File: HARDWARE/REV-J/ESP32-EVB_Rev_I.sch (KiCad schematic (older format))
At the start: 151 parts, among them CON1 TB3 DG306-5.0-3P, CON2 TB3 DG306-5.0-3P, Q1 BC817-40(SOT23), Q2 BC817-40(SOT23), Q3 Q12MHz/20pF/30ppm/2P/HC-49SM(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, Q4 BC817-40(SOT23), Q5 BC817-40(SOT23), Q7 BC817-40(SOT23), U1 BL4054B-42TPRN(SOT23-5), U10 BAT54C(SOT23-3), U2 SY8089AAAC(SOT23-5), U3 ESP-WROOM-32, U4 LAN8710A-EZC(QFN32), U5 CH340T(SSOP20W), U6 MCP2562-E/SN(SOIC-8_150mil), U7 RPM7236-H8, U8 NCP303LSN27T1G(SOT-23-5), U9 BAT54C(SOT23-3)

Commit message: Update 434121043836 (rev1).stp, 5040771891.stp, and 173 more files...
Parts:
- removed 5.0V/3.3V2: Closed(1-2)/Opened(2-3), OLIMEX_Jumpers-FP:SJ_2_SMALL_12_TIED, symbol ESP32-EVB_Rev_I:SJ2W_Closed(1-2)
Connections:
- net labels removed: vm
- wire segments 689 -> 690
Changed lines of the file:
@@
 	13900 13400 13900 13900
 Connection ~ 13900 13900
-Connection ~ 13700 13900
-Wire Wire Line
-	13000 13900 13700 13900
 Wire Wire Line
 	15600 13700 13000 13700
@@
 	13000 14000 15600 14000
 Wire Wire Line
-	13000 13800 13500 13800
-Wire Wire Line
-	13500 13800 13500 14900
+	13000 13800 13150 13800
 Wire Wire Line
 	19900 7800 18800 7800
@@
 	12400 14000 11600 14000
 Wire Wire Line
+	11600 14000 11600 14400
+Wire Wire Line
+	11600 14400 12600 14400
+Wire Wire Line
 	2900 1800 2900 2100
 Wire Wire Line
@@
 Wire Wire Line
 	13700 13900 13700 14500
+$Comp
+L ESP32-EVB_Rev_I:+3.3V #PWR0101
+U 1 1 5B27C8D3
+P 12600 14400
+F 0 "#PWR0101" H 12600 14250 50  0001 C CNN
+F 1 "+3.3V" V 12600 14525 50  0000 L CNN
+F 2 "" H 12600 14400 60  0000 C CNN
+F 3 "" H 12600 14400 60  0000 C CNN
+	1    12600 14400
+	0    1    1    0
+$EndComp
 $Comp
 L ESP32-EVB_Rev_I:MCP2562-E_SN(SOIC-8_150mil) U6
@@
 	-1   0    0    1
 $EndComp
-$Comp
-L ESP32-EVB_Rev_I:SJ2W_Closed(1-2) 5.0V/3.3V2
-U 1 1 6188D1A4
-P 12350 14650
-F 0 "5.0V/3.3V2" V 12650 14400 50  0000 L BNN
-F 1 "Closed(1-2)/Opened(2-3)" V 12550 14100 50  0000 L BNN
-F 2 "OLIMEX_Jumpers-FP:SJ_2_SMALL_12_TIED" H 12380 14800 20  0001 C CNN
-F 3 "" H 12350 14650 60  0000 C CNN
-	1    12350 14650
-	1    0    0    1
-$EndComp
-$Comp
-L ESP32-EVB_Rev_I:+3.3V #PWR0101
-U 1 1 5B27C8D3
-P 12350 14450
-F 0 "#PWR0101" H 12350 14300 50  0001 C CNN
-F 1 "+3.3V" H 12050 14500 50  0000 L CNN
-F 2 "" H 12350 14450 60  0000 C CNN
-F 3 "" H 12350 14450 60  0000 C CNN
-	1    12350 14450
-	1    0    0    -1
-$EndComp
-Wire Wire Line
-	12150 14650 11600 14650
-Wire Wire Line
-	11600 14000 11600 14650
-$Comp
-L ESP32-EVB_Rev_I:GND #PWR0114
-U 1 1 61ADEB7D
-P 12350 14850
-F 0 "#PWR0114" H 12350 14600 50  0001 C CNN
-F 1 "GND" H 12350 14700 50  0000 C CNN
-F 2 "" H 12350 14850 60  0000 C CNN
-F 3 "" H 12350 14850 60  0000 C CNN
-	1    12350 14850
-	1    0    0    -1
-$EndComp
-Connection ~ 11000 13800
+Wire Wire Line
+	13000 13900 13150 13900
+Wire Wire Line
+	13150 13800 13150 13900
+Wire Wire Line
+	11500 13600 11800 13600
+Connection ~ 11500 13600
+Connection ~ 11800 13600
 $Comp
 L ESP32-EVB_Rev_I:R R12
-U 1 1 61AF20A4
+U 1 1 61A8BD6D
 P 10850 13800
-F 0 "R12" H 10850 13800 50  0000 C CNN
-F 1 "10k/R0603" H 10750 13900 50  0000 C CNN
+F 0 "R12" H 11025 13850 50  0000 C CNN
+F 1 "10k/R0603" H 10525 13850 50  0000 C CNN
 F 2 "OLIMEX_RLC-FP:R_0603_5MIL_DWS" V 10780 13800 30  0001 C CNN
 F 3 "" H 10850 13800 30  0000 C CNN
 	1    10850 13800
-	1    0    0    1
-$EndComp
+	-1   0    0    -1
+$EndComp
+Connection ~ 11000 13800
 $Comp
 L ESP32-EVB_Rev_I:R R13
-U 1 1 61B8557C
-P 11000 14950
-F 0 "R13" H 11000 14950 50  0000 C CNN
-F 1 "10k/R0603" H 11100 14850 50  0000 C CNN
-F 2 "OLIMEX_RLC-FP:R_0603_5MIL_DWS" V 10930 14950 30  0001 C CNN
-F 3 "" H 11000 14950 30  0000 C CNN
-	1    11000 14950
-	0    -1   1    0
-$EndComp
-Connection ~ 11000 14800
-$Comp
-L ESP32-EVB_Rev_I:GND #PWR0115
-U 1 1 61B984EC
+U 1 1 61A8C506
+P 11650 14800
+F 0 "R13" H 11825 14850 50  0000 C CNN
+F 1 "10k/R0603" H 11325 14850 50  0000 C CNN
+F 2 "OLIMEX_RLC-FP:R_0603_5MIL_DWS" V 11580 14800 30  0001 C CNN
+F 3 "" H 11650 14800 30  0000 C CNN
+	1    11650 14800
+	-1   0    0    -1
+$EndComp
+Connection ~ 11500 14800
+$Comp
+L ESP32-EVB_Rev_I:GND #PWR0114
+U 1 1 61A8D549
 P 10700 13800
-F 0 "#PWR0115" H 10700 13550 50  0001 C CNN
-F 1 "GND" V 10700 13625 50  0000 C CNN
+F 0 "#PWR0114" H 10700 13550 50  0001 C CNN
+F 1 "GND" H 10700 13650 50  0000 C CNN
 F 2 "" H 10700 13800 60  0000 C CNN
 F 3 "" H 10700 13800 60  0000 C CNN
 	1    10700 13800
-	0    1    -1   0
-$EndComp
-Text GLabel 11000 15100 3    50   Input ~ 0
-vm
-Text Label 12300 13700 0    50   ~ 0
-vm
+	1    0    0    -1
+$EndComp
 $EndSCHEMATC

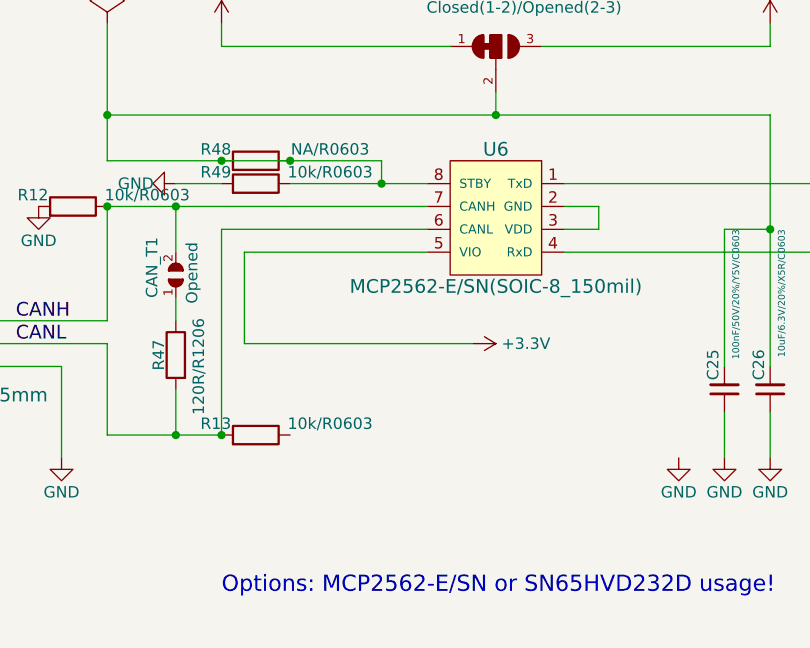
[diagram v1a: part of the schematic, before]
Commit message: Update ESP32-EVB_Rev_I.sch, ESP32-EVB_Rev_I.sch-bak, and _autosave-ESP32-EVB_Rev_I.sch
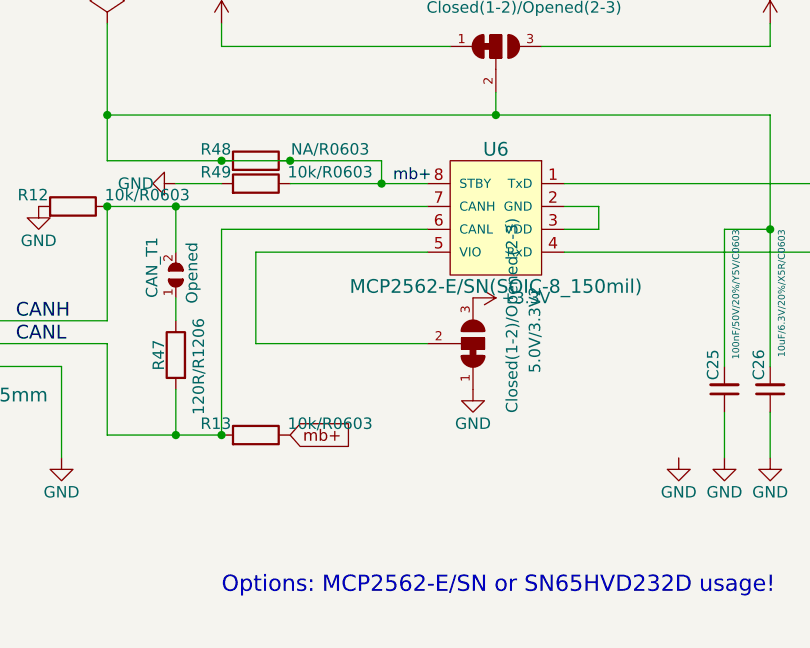
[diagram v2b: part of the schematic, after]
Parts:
- added 5.0V/3.3V2: Closed(1-2)/Opened(2-3), OLIMEX_Jumpers-FP:SJ_2_SMALL_12_TIED, symbol ESP32-EVB_Rev_I:SJ2W_Closed(1-2)
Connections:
- net labels added: mb+
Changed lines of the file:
@@
 Options: MCP2562-E/SN or SN65HVD232D usage!
-Wire Wire Line
-	12400 14000 11600 14000
-Wire Wire Line
-	11600 14000 11600 14400
-Wire Wire Line
-	11600 14400 12600 14400
 Wire Wire Line
 	2900 1800 2900 2100
@@
 Wire Wire Line
 	13700 13900 13700 14500
-$Comp
-L ESP32-EVB_Rev_I:+3.3V #PWR0101
-U 1 1 5B27C8D3
-P 12600 14400
-F 0 "#PWR0101" H 12600 14250 50  0001 C CNN
-F 1 "+3.3V" V 12600 14525 50  0000 L CNN
-F 2 "" H 12600 14400 60  0000 C CNN
-F 3 "" H 12600 14400 60  0000 C CNN
-	1    12600 14400
-	0    1    1    0
-$EndComp
 $Comp
 L ESP32-EVB_Rev_I:MCP2562-E_SN(SOIC-8_150mil) U6
@@
 	1    0    0    -1
 $EndComp
+Text Label 12250 13700 0    50   ~ 0
+mb+
+Text GLabel 11800 14800 2    50   Input ~ 0
+mb+
+$Comp
+L ESP32-EVB_Rev_I:+3.3V #PWR0101
+U 1 1 5B27C8D3
+P 12600 14200
+F 0 "#PWR0101" H 12600 14050 50  0001 C CNN
+F 1 "+3.3V" V 12600 14325 50  0000 L CNN
+F 2 "" H 12600 14200 60  0000 C CNN
+F 3 "" H 12600 14200 60  0000 C CNN
+	1    12600 14200
+	0    1    1    0
+$EndComp
+$Comp
+L ESP32-EVB_Rev_I:SJ2W_Closed(1-2) 5.0V/3.3V2
+U 1 1 61B60BDC
+P 12600 14400
+F 0 "5.0V/3.3V2" V 12900 14150 50  0000 L BNN
+F 1 "Closed(1-2)/Opened(2-3)" V 12800 13850 50  0000 L BNN
+F 2 "OLIMEX_Jumpers-FP:SJ_2_SMALL_12_TIED" H 12630 14550 20  0001 C CNN
+F 3 "" H 12600 14400 60  0000 C CNN
+	1    12600 14400
+	1    0    0    1
+$EndComp
+$Comp
+L ESP32-EVB_Rev_I:GND #PWR0115
+U 1 1 61C899C9
+P 12600 14600
+F 0 "#PWR0115" H 12600 14350 50  0001 C CNN
+F 1 "GND" H 12600 14450 50  0000 C CNN
+F 2 "" H 12600 14600 60  0000 C CNN
+F 3 "" H 12600 14600 60  0000 C CNN
+	1    12600 14600
+	1    0    0    -1
+$EndComp
+Wire Wire Line
+	12400 14400 11650 14400
+Wire Wire Line
+	11650 14400 11650 14000
+Wire Wire Line
+	11650 14000 12400 14000
 $EndSCHEMATC

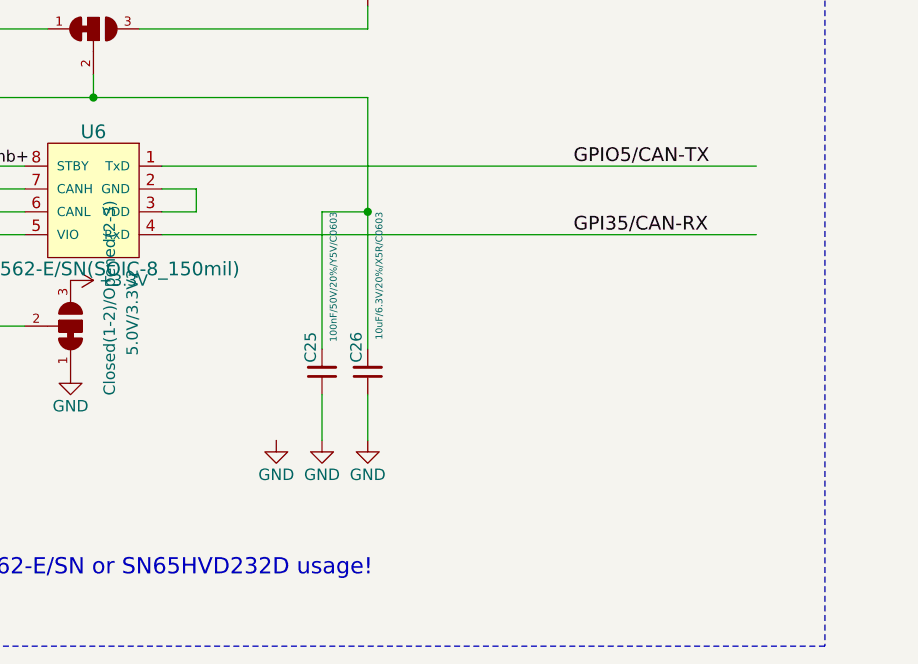
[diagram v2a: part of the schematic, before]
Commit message: Update ESP32-EVB_Rev_I-cache.lib, ESP32-EVB_Rev_I.kicad_pcb, and 3 more files...
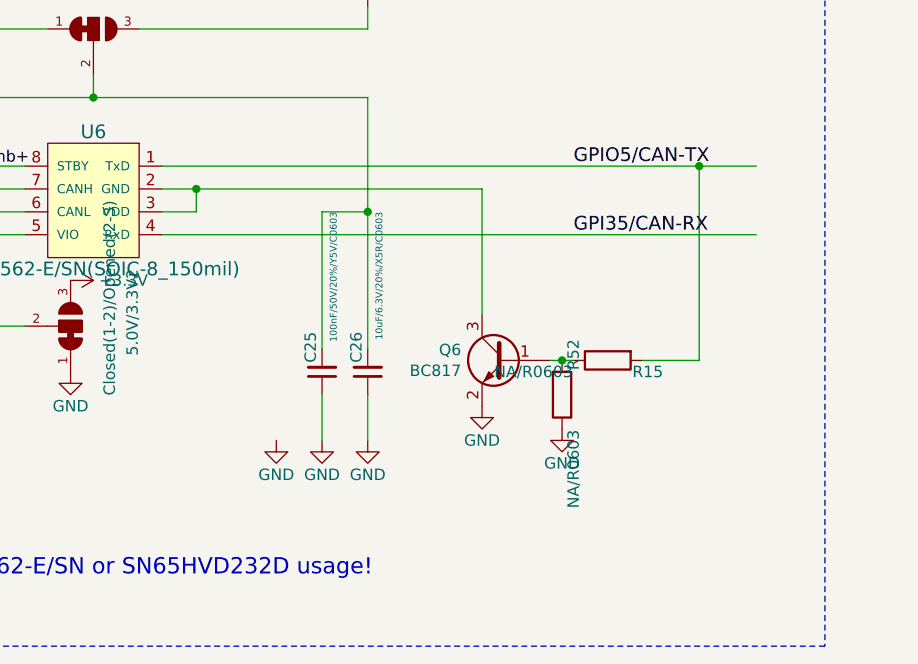
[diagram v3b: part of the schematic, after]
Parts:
- added Q6: BC817, Package_TO_SOT_SMD:SOT-23, symbol Transistor_BJT:BC817
- added R15, R52: NA/R0603, OLIMEX_RLC-FP:R_0603_5MIL_DWS, symbol ESP32-EVB_Rev_I:R
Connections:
- wire segments 690 -> 697
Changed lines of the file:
@@
 Connection ~ 13900 13900
 Wire Wire Line
-	15600 13700 13000 13700
+	15600 13700 15350 13700
 Wire Wire Line
 	13000 14000 15600 14000
@@
 Wire Wire Line
 	11650 14000 12400 14000
+$Comp
+L Transistor_BJT:BC817 Q6
+U 1 1 6144F6FA
+P 14500 14550
+F 0 "Q6" H 14691 14596 50  0000 L CNN
+F 1 "BC817" H 14691 14505 50  0000 L CNN
+F 2 "Package_TO_SOT_SMD:SOT-23" H 14700 14475 50  0001 L CIN
+F 3 "https://www.onsemi.com/pub/Collateral/BC818-D.pdf" H 14500 14550 50  0001 L CNN
+	1    14500 14550
+	-1   0    0    -1
+$EndComp
+Wire Wire Line
+	13150 13800 14400 13800
+Wire Wire Line
+	14400 13800 14400 14350
+Connection ~ 13150 13800
+$Comp
+L ESP32-EVB_Rev_I:GND #PWR0116
+U 1 1 616A1F1A
+P 14400 14750
+F 0 "#PWR0116" H 14400 14500 50  0001 C CNN
+F 1 "GND" H 14400 14600 50  0000 C CNN
+F 2 "" H 14400 14750 60  0000 C CNN
+F 3 "" H 14400 14750 60  0000 C CNN
+	1    14400 14750
+	1    0    0    -1
+$EndComp
+$Comp
+L ESP32-EVB_Rev_I:GND #PWR0117
+U 1 1 6176ED66
+P 14750 14850
+F 0 "#PWR0117" H 14750 14600 50  0001 C CNN
+F 1 "GND" H 14750 14700 50  0000 C CNN
+F 2 "" H 14750 14850 60  0000 C CNN
+F 3 "" H 14750 14850 60  0000 C CNN
+	1    14750 14850
+	1    0    0    -1
+$EndComp
+Wire Wire Line
+	15100 14550 15350 14550
+Wire Wire Line
+	15350 14550 15350 13700
+Connection ~ 15350 13700
+Wire Wire Line
+	15350 13700 13000 13700
+Wire Wire Line
+	14700 14550 14750 14550
+$Comp
+L ESP32-EVB_Rev_I:R R52
+U 1 1 618069C7
+P 14750 14700
+F 0 "R52" H 14925 14750 50  0000 C CNN
+F 1 "NA/R0603" H 14425 14750 50  0000 C CNN
+F 2 "OLIMEX_RLC-FP:R_0603_5MIL_DWS" V 14680 14700 30  0001 C CNN
+F 3 "" H 14750 14700 30  0000 C CNN
+	1    14750 14700
+	0    1    -1   0
+$EndComp
+Connection ~ 14750 14550
+Wire Wire Line
+	14750 14550 14800 14550
+$Comp
+L ESP32-EVB_Rev_I:R R15
+U 1 1 618086CA
+P 14950 14550
+F 0 "R15" H 15125 14600 50  0000 C CNN
+F 1 "NA/R0603" H 14625 14600 50  0000 C CNN
+F 2 "OLIMEX_RLC-FP:R_0603_5MIL_DWS" V 14880 14550 30  0001 C CNN
+F 3 "" H 14950 14550 30  0000 C CNN
+	1    14950 14550
+	1    0    0    1
+$EndComp
 $EndSCHEMATC

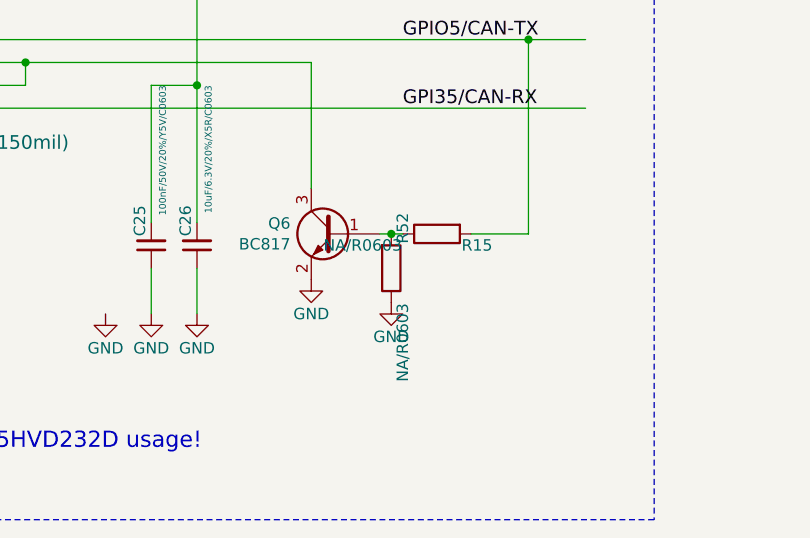
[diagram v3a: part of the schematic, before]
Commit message: fix auto control flow modbus
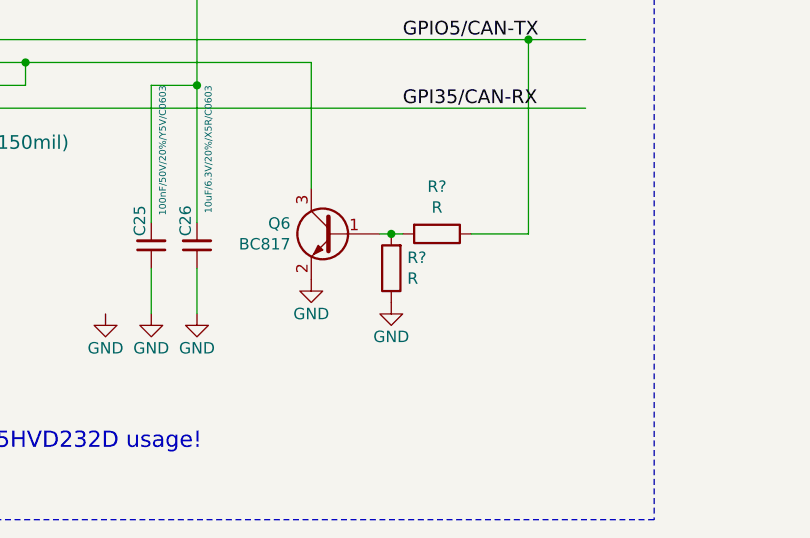
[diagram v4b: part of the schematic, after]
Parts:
- removed R15, R52: NA/R0603, OLIMEX_RLC-FP:R_0603_5MIL_DWS, symbol ESP32-EVB_Rev_I:R
- added R? (x2): R, Resistor_SMD:R_0603_1608Metric, symbol Device:R
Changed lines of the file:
@@
 	14700 14550 14750 14550
 $Comp
-L ESP32-EVB_Rev_I:R R52
-U 1 1 618069C7
+L Device:R R?
+U 1 1 614C248B
+P 14950 14550
+F 0 "R?" V 14743 14550 50  0000 C CNN
+F 1 "R" V 14834 14550 50  0000 C CNN
+F 2 "Resistor_SMD:R_0603_1608Metric" V 14880 14550 50  0001 C CNN
+F 3 "~" H 14950 14550 50  0001 C CNN
+	1    14950 14550
+	0    1    1    0
+$EndComp
+$Comp
+L Device:R R?
+U 1 1 614C4787
 P 14750 14700
-F 0 "R52" H 14925 14750 50  0000 C CNN
-F 1 "NA/R0603" H 14425 14750 50  0000 C CNN
-F 2 "OLIMEX_RLC-FP:R_0603_5MIL_DWS" V 14680 14700 30  0001 C CNN
-F 3 "" H 14750 14700 30  0000 C CNN
+F 0 "R?" H 14680 14654 50  0000 R CNN
+F 1 "R" H 14680 14745 50  0000 R CNN
+F 2 "Resistor_SMD:R_0603_1608Metric" V 14680 14700 50  0001 C CNN
+F 3 "~" H 14750 14700 50  0001 C CNN
 	1    14750 14700
-	0    1    -1   0
+	-1   0    0    1
 $EndComp
 Connection ~ 14750 14550
 Wire Wire Line
 	14750 14550 14800 14550
-$Comp
-L ESP32-EVB_Rev_I:R R15
-U 1 1 618086CA
-P 14950 14550
-F 0 "R15" H 15125 14600 50  0000 C CNN
-F 1 "NA/R0603" H 14625 14600 50  0000 C CNN
-F 2 "OLIMEX_RLC-FP:R_0603_5MIL_DWS" V 14880 14550 30  0001 C CNN
-F 3 "" H 14950 14550 30  0000 C CNN
-	1    14950 14550
-	1    0    0    1
-$EndComp
 $EndSCHEMATC

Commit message: Update ESP32-EVB_Rev_I-cache.lib, ESP32-EVB_Rev_I.kicad_pcb, and 4 more files...
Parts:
- removed 5.0V/3.3V2: Closed(1-2)/Opened(2-3), OLIMEX_Jumpers-FP:SJ_2_SMALL_12_TIED, symbol ESP32-EVB_Rev_I:SJ2W_Closed(1-2)
- added JP1: SolderJumper_3_Bridged12, Jumper:SolderJumper-3_P1.3mm_Bridged2Bar12_Pad1.0x1.5mm_NumberLabels, symbol Jumper:SolderJumper_3_Bridged12
- added R58: R, Resistor_SMD:R_0603_1608Metric, symbol Device:R
- gave numbers to parts that had none: 2
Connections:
- wire segments 697 -> 700
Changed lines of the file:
@@
-$EndComp
-$Comp
-L ESP32-EVB_Rev_I:SJ2W_Closed(1-2) 5.0V/3.3V2
-U 1 1 61B60BDC
-P 12600 14400
-F 0 "5.0V/3.3V2" V 12900 14150 50  0000 L BNN
-F 1 "Closed(1-2)/Opened(2-3)" V 12800 13850 50  0000 L BNN
-F 2 "OLIMEX_Jumpers-FP:SJ_2_SMALL_12_TIED" H 12630 14550 20  0001 C CNN
-F 3 "" H 12600 14400 60  0000 C CNN
-	1    12600 14400
-	1    0    0    1
 $EndComp
 $Comp
@@
 	1    0    0    -1
 $EndComp
-Wire Wire Line
-	12400 14400 11650 14400
 Wire Wire Line
 	11650 14400 11650 14000
@@
 	13150 13800 14400 13800
 Wire Wire Line
-	14400 13800 14400 14350
+	14400 13800 14400 13900
 Connection ~ 13150 13800
 $Comp
@@
 	14700 14550 14750 14550
 $Comp
-L Device:R R?
+L Device:R R15
 U 1 1 614C248B
 P 14950 14550
-F 0 "R?" V 14743 14550 50  0000 C CNN
+F 0 "R15" V 14743 14550 50  0000 C CNN
 F 1 "R" V 14834 14550 50  0000 C CNN
 F 2 "Resistor_SMD:R_0603_1608Metric" V 14880 14550 50  0001 C CNN
@@
 $EndComp
 $Comp
-L Device:R R?
+L Device:R R52
 U 1 1 614C4787
 P 14750 14700
-F 0 "R?" H 14680 14654 50  0000 R CNN
+F 0 "R52" H 14680 14654 50  0000 R CNN
 F 1 "R" H 14680 14745 50  0000 R CNN
 F 2 "Resistor_SMD:R_0603_1608Metric" V 14680 14700 50  0001 C CNN
@@
 Wire Wire Line
 	14750 14550 14800 14550
+$Comp
+L Device:R R58
+U 1 1 614C9259
+P 14200 13900
+F 0 "R58" V 14407 13900 50  0000 C CNN
+F 1 "R" V 14316 13900 50  0000 C CNN
+F 2 "Resistor_SMD:R_0603_1608Metric" V 14130 13900 50  0001 C CNN
+F 3 "~" H 14200 13900 50  0001 C CNN
+	1    14200 13900
+	0    -1   -1   0
+$EndComp
+Wire Wire Line
+	14050 13900 13900 13900
+Wire Wire Line
+	14350 13900 14400 13900
+Connection ~ 14400 13900
+Wire Wire Line
+	14400 13900 14400 14350
+$Comp
+L Jumper:SolderJumper_3_Bridged12 JP1
+U 1 1 616705BA
+P 12600 14400
+F 0 "JP1" V 12646 14468 50  0000 L CNN
+F 1 "SolderJumper_3_Bridged12" V 12555 14468 50  0000 L CNN
+F 2 "Jumper:SolderJumper-3_P1.3mm_Bridged2Bar12_Pad1.0x1.5mm_NumberLabels" H 12600 14400 50  0001 C CNN
+F 3 "~" H 12600 14400 50  0001 C CNN
+	1    12600 14400
+	0    1    -1   0
+$EndComp
+Wire Wire Line
+	11650 14400 12450 14400
 $EndSCHEMATC
